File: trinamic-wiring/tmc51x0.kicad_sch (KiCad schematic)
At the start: 0 parts

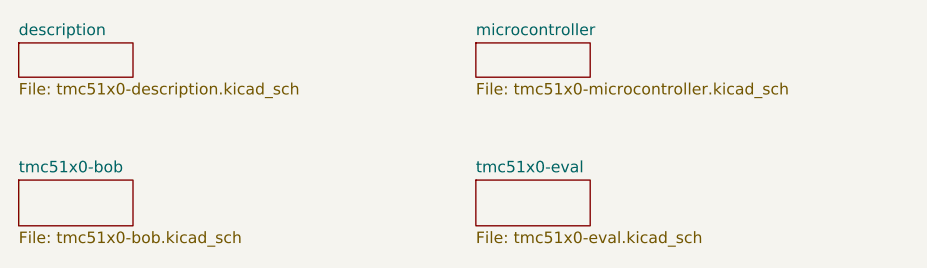
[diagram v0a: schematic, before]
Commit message: Split tmc51x0 into spi and uart
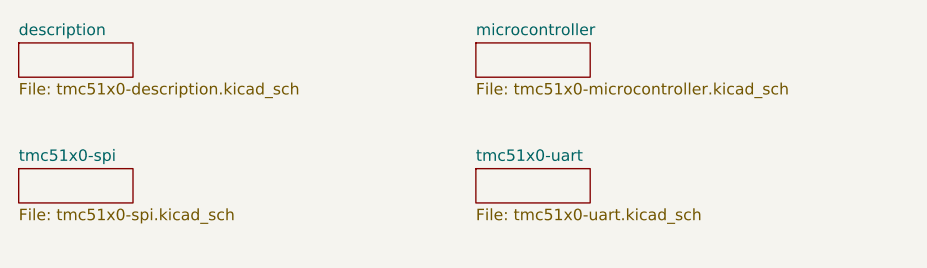
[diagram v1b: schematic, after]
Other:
- removed sheet tmc51x0-bob
- removed sheet tmc51x0-eval
- added sheet tmc51x0-spi (tmc51x0-spi.kicad_sch)
- added sheet tmc51x0-uart (tmc51x0-uart.kicad_sch)
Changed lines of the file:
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@@
   (title_block
     (title "Trinamic Wiring")
-    (date "2024-07-31")
+    (date "2024-08-01")
     (rev "0.5")
     (company "Janelia Research Campus")
-  )
-  (sheet (at 43.18 68.58) (size 12.7 5.08) (fields_autoplaced)
-    (stroke (width 0.1524) (type solid))
-    (fill (color 0 0 0 0.0000))
-    (property "Sheetname" "tmc51x0-bob" (at 43.18 67.8684 0)
-      (effects (font (size 1.27 1.27)) (justify left bottom))
-    )
-    (property "Sheetfile" "tmc51x0-bob.kicad_sch" (at 43.18 74.2446 0)
-      (effects (font (size 1.27 1.27)) (justify left top))
-    )
-    (instances
-      (project "trinamic-wiring"
-        (path "/e4144788-6304-493f-818e-5d881d3b7418/a161638e-a96f-4455-865a-1d7502675f43" (page "30"))
-      )
-    )
   )
   (sheet (at 43.18 53.34) (size 12.7 3.81) (fields_autoplaced)
@@
     )
   )
-  (sheet (at 93.98 68.58) (size 12.7 5.08) (fields_autoplaced)
+  (sheet (at 93.98 67.31) (size 12.7 3.81) (fields_autoplaced)
     (stroke (width 0.1524) (type solid))
     (fill (color 0 0 0 0.0000))
-    (property "Sheetname" "tmc51x0-eval" (at 93.98 67.8684 0)
+    (property "Sheetname" "tmc51x0-uart" (at 93.98 66.5984 0)
       (effects (font (size 1.27 1.27)) (justify left bottom))
     )
-    (property "Sheetfile" "tmc51x0-eval.kicad_sch" (at 93.98 74.2446 0)
+    (property "Sheetfile" "tmc51x0-uart.kicad_sch" (at 93.98 71.7046 0)
       (effects (font (size 1.27 1.27)) (justify left top))
     )
     (instances
       (project "trinamic-wiring"
-        (path "/e4144788-6304-493f-818e-5d881d3b7418/a161638e-a96f-4455-865a-1d7502675f43" (page "18"))
+        (path "/e4144788-6304-493f-818e-5d881d3b7418/a161638e-a96f-4455-865a-1d7502675f43" (page "20"))
       )
     )
+  )
+  (sheet (at 43.18 67.31) (size 12.7 3.81) (fields_autoplaced)
+    (stroke (width 0.1524) (type solid))
+    (fill (color 0 0 0 0.0000))
+    (property "Sheetname" "tmc51x0-spi" (at 43.18 66.5984 0)
+      (effects (font (size 1.27 1.27)) (justify left bottom))
+    )
+    (property "Sheetfile" "tmc51x0-spi.kicad_sch" (at 43.18 71.7046 0)
+      (effects (font (size 1.27 1.27)) (justify left top))
+    )
+    (instances
+      (project "trinamic-wiring"
+        (path "/e4144788-6304-493f-818e-5d881d3b7418/a161638e-a96f-4455-865a-1d7502675f43" (page "24"))
+      )
+    )
